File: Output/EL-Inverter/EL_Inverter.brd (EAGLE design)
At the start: 20 x 13 mm, 11 parts, among them Q1 MMBT5088, Q2 MMBT5088, Q3 MMBT5088

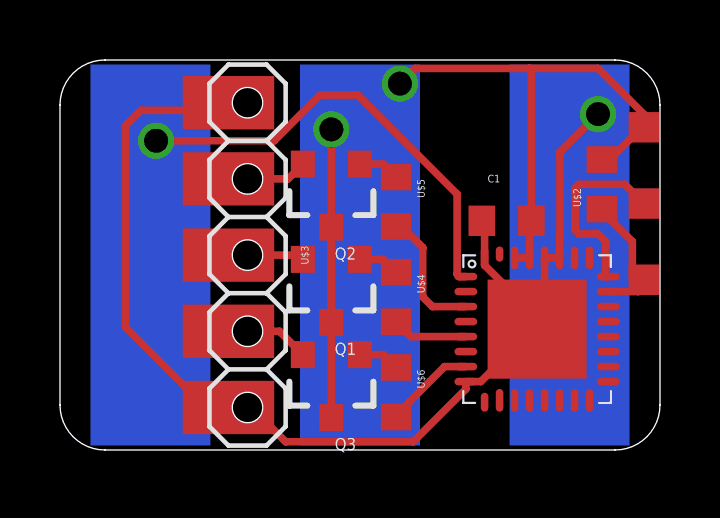
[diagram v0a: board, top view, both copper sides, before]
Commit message: Update Pinheader
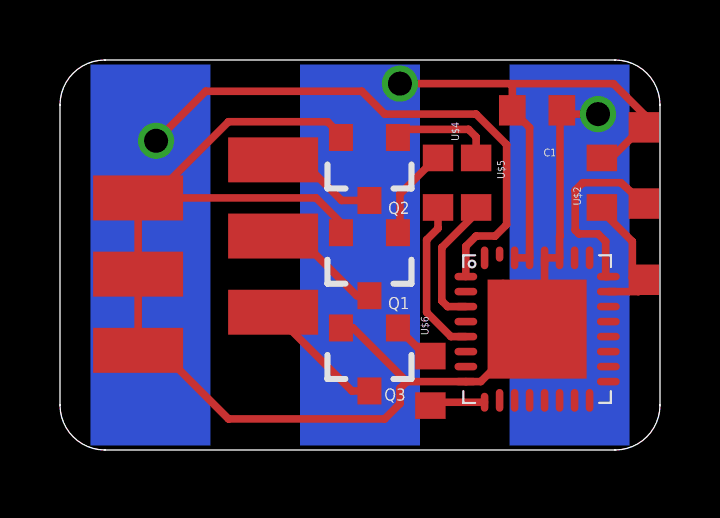
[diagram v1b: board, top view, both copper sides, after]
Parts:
- removed U$3: PINHD_52.54MOD, thar:PINHD_5_MOD
- added U$7: PINHD_6MICROMATCH, thar:MICROMATCH6POL
- moved U$4 4.06 mm to (14.4, 10.2)
- moved C1 3.82 mm to (17.7, 12.6), turned to 0 degrees
- moved U$5 2.74 mm to (15.6, 10.2)
- moved Q1 1.55 mm to (12.1, 7.49)
- moved Q3 1.55 mm to (12.1, 4.32)
- moved Q2 1.55 mm to (12.1, 10.7)
- moved U$6 1.20 mm to (14.1, 3.56)
- moved U$2 0.05 mm to (19.8, 10.2)
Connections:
- net GND: now also Q1.2, Q2.2, Q3.2, U$7.P$2, U$7.P$4, U$7.P$6; no longer U$10.32, U$3.P$1, U$3.P$5
- net N$13: now also Q3.3, U$7.P$5; no longer Q3.2, U$3.P$4
- net N$17: now also U$10.9; no longer U$10.7
- net N$6: now also Q2.3, U$7.P$1; no longer Q2.2, U$3.P$2
- net N$7: now also Q1.3, U$7.P$3; no longer Q1.2, U$3.P$3
- net VCC: no longer Q1.3, Q2.3, Q3.3
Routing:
- net VCC: track 39.1 -> 25.7 mm, vias 2 -> 1
- net GND: track 53.2 -> 63.5 mm
- net N$12: track 21.8 -> 25.2 mm
- net N$16: track 2.53 -> 5.29 mm
- net N$5: track 1.39 -> 3.52 mm
- net N$2: track 1.39 -> 3.08 mm
- net N$13: track 2.80 -> 4.30 mm
- net N$7: track 2.54 -> 4.03 mm
- net N$17: track 3.04 -> 1.85 mm
- net N$6: track 2.68 -> 3.77 mm
